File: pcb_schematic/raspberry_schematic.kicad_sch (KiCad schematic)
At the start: 13 parts, among them J1 Raspberry_Pi_2_3, SW1 SW_Push, SW2 SW_Push, SW3 SW_Push, SW4 SW_Push

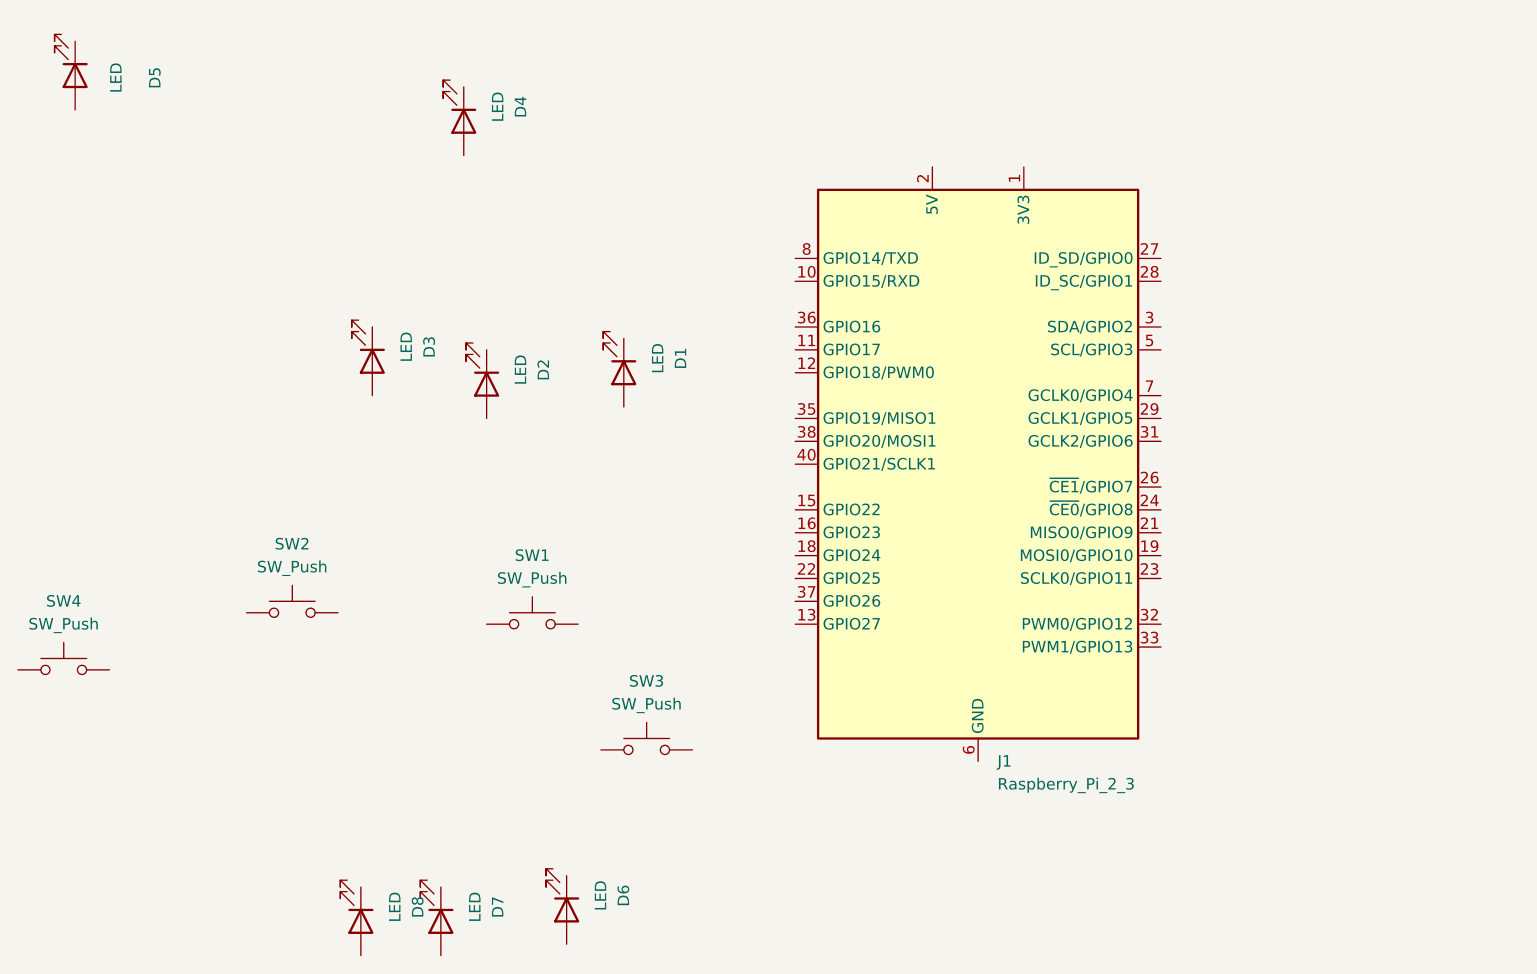
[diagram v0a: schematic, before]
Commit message: Finished raspberry schematic
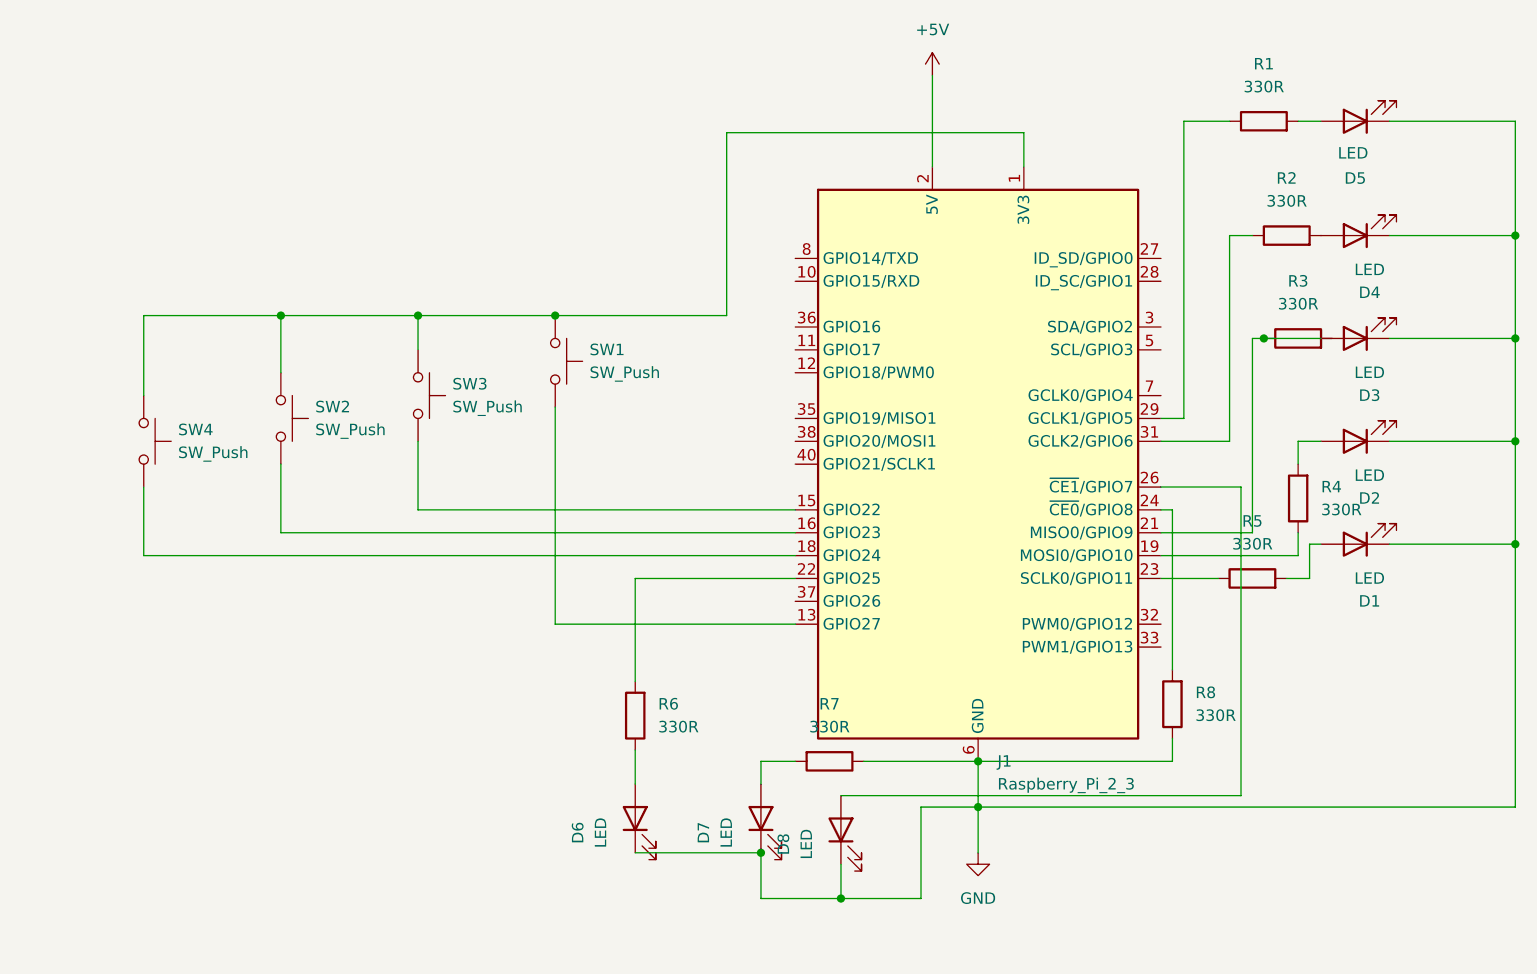
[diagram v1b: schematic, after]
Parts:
- added R1, R2, R3, R4, R5, R6, R7, R8: 330R, symbol Device:R
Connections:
- net at SW3.1: now also J1.1 (3V3), J1.17 (3V3), SW1.1, SW2.1, SW4.1
- net at SW3.2: now also J1.15 (GPIO22)
- net GND: now reaches D8.1 (K)
- net GND: now also D1.1 (K), D2.1 (K), D3.1 (K), D4.1 (K), D5.1 (K), D6.1 (K), D7.1 (K), J1.14 (GND), J1.20 (GND), J1.25 (GND), J1.30 (GND), J1.34 (GND), J1.39 (GND), J1.6 (GND), J1.9 (GND), R7.1, R8.1
- net at D8.2 (A): now also J1.26 (~{CE1}/GPIO7)
- net at D1.2 (A): now also R5.2
- net at D7.2 (A): now also R7.2
- net at D4.2 (A): now also R2.2
- net at D5.2 (A): now also R1.2
- net at D3.2 (A): now also J1.21 (MISO0/GPIO9), R3.1
- net at SW2.2: now also J1.16 (GPIO23)
- net at J1.13 (GPIO27): now also SW1.2
- net at J1.18 (GPIO24): now also SW4.2
- net at J1.19 (MOSI0/GPIO10): now also R4.1
- net +5V: now reaches J1.2 (5V), J1.4 (5V)
- net at J1.22 (GPIO25): now also R6.2
- net at J1.23 (SCLK0/GPIO11): now also R5.1
- net at J1.24 (~{CE0}/GPIO8): now also R8.2
- net at J1.29 (GCLK1/GPIO5): now also R1.1
- net at J1.31 (GCLK2/GPIO6): now also R2.1
- net at D6.2 (A): now also R6.1
- net at D2.2 (A): now also R4.2
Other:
- moved on the sheet: D1, D2, D3, D4, D5, D6, D7, D8, SW1, SW2, SW3, SW4

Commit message: Changed raspberry schematic to use currently available resistors
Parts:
- removed R6: 330R, symbol Device:R
- added R10, R11, R12, R13, R14, R15, R16, R9: 47R, symbol Device:R
- added R17, R18, R19: 10R, symbol Device:R
- R1, R2, R3, R4, R5, R8: value 330R -> 15R
- R7: value 330R -> 10R
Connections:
- net GND: now also R14.1, R17.1; no longer R7.1, R8.1
- net at D8.2 (A): now also R8.1; no longer J1.26 (~{CE1}/GPIO7)
- net at R5.1: now also R13.1; no longer J1.23 (SCLK0/GPIO11)
- net at R3.2: now also D3.2 (A)
- net at J1.24 (~{CE0}/GPIO8): now also R14.2; no longer R8.2
- net at J1.29 (GCLK1/GPIO5): now also R9.1; no longer R1.1
- net at J1.19 (MOSI0/GPIO10): now also R12.2; no longer R4.1
- net at J1.22 (GPIO25): now also R15.1
- net at J1.31 (GCLK2/GPIO6): now also R10.1; no longer R2.1
- net at D6.2 (A): now also R19.2
- new net: J1.23 (SCLK0/GPIO11), R13.2
- new net: R1.1, R9.2
- new net: R17.2, R7.1
- new net: R10.2, R2.1
- new net: R15.2, R18.1
- new net: R18.2, R19.1
- new net: J1.21 (MISO0/GPIO9), R11.1
- new net: J1.26 (~{CE1}/GPIO7), R16.2
- new net: R16.1, R8.2
- new net: R11.2, R3.1
- new net: R12.1, R4.1
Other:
- moved on the sheet: D1, D2, D3, R4, R5

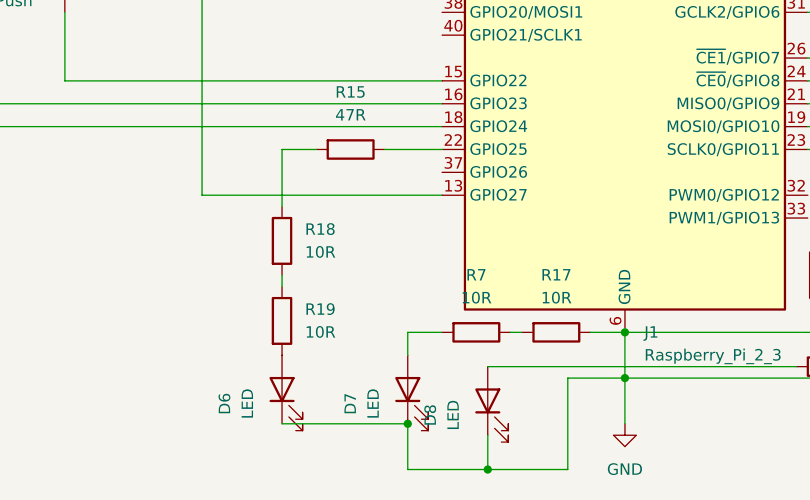
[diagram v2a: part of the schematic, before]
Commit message: Found 2 more 15 ohm resistors to use instead of 2 10 ohm resistors
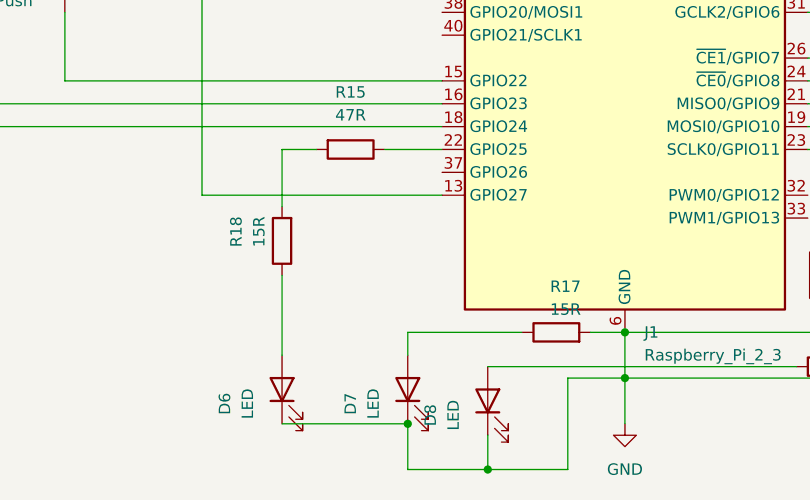
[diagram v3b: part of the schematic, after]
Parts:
- removed R19, R7: 10R, symbol Device:R
- R17, R18: value 10R -> 15R
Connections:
- net GND: now also R17.2; no longer R17.1
- net at D7.2 (A): now also R17.1
- net at R18.1: now also D6.2 (A); no longer R15.2
- net at R18.2: now also R15.2
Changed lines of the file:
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@@
-	(wire
-		(pts
-			(xy 154.94 142.24) (xy 156.21 142.24)
-		)
-		(stroke
-			(width 0)
-			(type default)
-		)
-	)
 	(wire
 		(pts
@@
 	(wire
 		(pts
+			(xy 129.54 135.89) (xy 129.54 144.78)
+		)
+		(stroke
+			(width 0)
+			(type default)
+		)
+	)
+	(wire
+		(pts
 			(xy 195.58 87.63) (xy 195.58 83.82)
 		)
@@
 	(wire
 		(pts
-			(xy 143.51 142.24) (xy 147.32 142.24)
-		)
-		(stroke
-			(width 0)
-			(type default)
-		)
-	)
-	(wire
-		(pts
-			(xy 129.54 135.89) (xy 129.54 137.16)
+			(xy 143.51 142.24) (xy 156.21 142.24)
 		)
 		(stroke
@@
 	)
 	(symbol
-		(lib_id "Device:R")
-		(at 160.02 142.24 270)
-		(unit 1)
-		(exclude_from_sim no)
-		(in_bom yes)
-		(on_board yes)
-		(dnp no)
-		(fields_autoplaced yes)
-		(property "Reference" "R17"
-			(at 160.02 135.89 90)
-			(effects
-				(font
-					(size 1.27 1.27)
-				)
-			)
-		)
-		(property "Value" "10R"
-			(at 160.02 138.43 90)
-			(effects
-				(font
-					(size 1.27 1.27)
-				)
-			)
-		)
-		(property "Footprint" ""
-			(at 160.02 140.462 90)
-			(effects
-				(font
-					(size 1.27 1.27)
-				)
-				(hide yes)
-			)
-		)
-		(property "Datasheet" "~"
-			(at 160.02 142.24 0)
-			(effects
-				(font
-					(size 1.27 1.27)
-				)
-				(hide yes)
-			)
-		)
-		(property "Description" "Resistor"
-			(at 160.02 142.24 0)
-			(effects
-				(font
-					(size 1.27 1.27)
-				)
-				(hide yes)
-			)
-		)
-		(pin "1"
-		)
-		(pin "2"
-		)
-		(instances
-			(project "raspberry_schematic"
-				(path "/b388c4a0-17e4-4175-bd7c-8be91d2c0837"
-					(reference "R17")
-					(unit 1)
-				)
-			)
-		)
-	)
-	(symbol
 		(lib_id "power:GND")
 		(at 167.64 152.4 0)
@@
 	(symbol
 		(lib_id "Device:R")
+		(at 129.54 132.08 180)
+		(unit 1)
+		(exclude_from_sim no)
+		(in_bom yes)
+		(on_board yes)
+		(dnp no)
+		(property "Reference" "R18"
+			(at 124.46 131.064 90)
+			(effects
+				(font
+					(size 1.27 1.27)
+				)
+			)
+		)
+		(property "Value" "15R"
+			(at 127 131.064 90)
+			(effects
+				(font
+					(size 1.27 1.27)
+				)
+			)
+		)
+		(property "Footprint" ""
+			(at 131.318 132.08 90)
+			(effects
+				(font
+					(size 1.27 1.27)
+				)
+				(hide yes)
+			)
+		)
+		(property "Datasheet" "~"
+			(at 129.54 132.08 0)
+			(effects
+				(font
+					(size 1.27 1.27)
+				)
+				(hide yes)
+			)
+		)
+		(property "Description" "Resistor"
+			(at 129.54 132.08 0)
+			(effects
+				(font
+					(size 1.27 1.27)
+				)
+				(hide yes)
+			)
+		)
+		(pin "1"
+		)
+		(pin "2"
+		)
+		(instances
+			(project "raspberry_schematic"
+				(path "/b388c4a0-17e4-4175-bd7c-8be91d2c0837"
+					(reference "R18")
+					(unit 1)
+				)
+			)
+		)
+	)
+	(symbol
+		(lib_id "Device:R")
 		(at 195.58 91.44 180)
 		(unit 1)
@@
 	)
 	(symbol
-		(lib_id "Device:R")
-		(at 151.13 142.24 270)
-		(unit 1)
-		(exclude_from_sim no)
-		(in_bom yes)
-		(on_board yes)
-		(dnp no)
-		(fields_autoplaced yes)
-		(property "Reference" "R7"
-			(at 151.13 135.89 90)
-			(effects
-				(font
-					(size 1.27 1.27)
-				)
-			)
-		)
-		(property "Value" "10R"
-			(at 151.13 138.43 90)
-			(effects
-				(font
-					(size 1.27 1.27)
-				)
-			)
-		)
-		(property "Footprint" ""
-			(at 151.13 140.462 90)
-			(effects
-				(font
-					(size 1.27 1.27)
-				)
-				(hide yes)
-			)
-		)
-		(property "Datasheet" "~"
-			(at 151.13 142.24 0)
-			(effects
-				(font
-					(size 1.27 1.27)
-				)
-				(hide yes)
-			)
-		)
-		(property "Description" "Resistor"
-			(at 151.13 142.24 0)
-			(effects
-				(font
-					(size 1.27 1.27)
-				)
-				(hide yes)
-			)
-		)
-		(pin "1"
-		)
-		(pin "2"
-		)
-		(instances
-			(project "raspberry_schematic"
-				(path "/b388c4a0-17e4-4175-bd7c-8be91d2c0837"
-					(reference "R7")
-					(unit 1)
-				)
-			)
-		)
-	)
-	(symbol
 		(lib_id "Device:LED")
 		(at 209.55 71.12 180)
@@
 	)
 	(symbol
-		(lib_id "Device:R")
-		(at 129.54 140.97 0)
-		(unit 1)
-		(exclude_from_sim no)
-		(in_bom yes)
-		(on_board yes)
-		(dnp no)
-		(fields_autoplaced yes)
-		(property "Reference" "R19"
-			(at 132.08 139.6999 0)
-			(effects
-				(font
-					(size 1.27 1.27)
-				)
-				(justify left)
-			)
-		)
-		(property "Value" "10R"
-			(at 132.08 142.2399 0)
-			(effects
-				(font
-					(size 1.27 1.27)
-				)
-				(justify left)
-			)
-		)
-		(property "Footprint" ""
-			(at 127.762 140.97 90)
-			(effects
-				(font
-					(size 1.27 1.27)
-				)
-				(hide yes)
-			)
-		)
-		(property "Datasheet" "~"
-			(at 129.54 140.97 0)
-			(effects
-				(font
-					(size 1.27 1.27)
-				)
-				(hide yes)
-			)
-		)
-		(property "Description" "Resistor"
-			(at 129.54 140.97 0)
-			(effects
-				(font
-					(size 1.27 1.27)
-				)
-				(hide yes)
-			)
-		)
-		(pin "1"
-		)
-		(pin "2"
-		)
-		(instances
-			(project "raspberry_schematic"
-				(path "/b388c4a0-17e4-4175-bd7c-8be91d2c0837"
-					(reference "R19")
-					(unit 1)
-				)
-			)
-		)
-	)
-	(symbol
 		(lib_id "Switch:SW_Push")
 		(at 90.17 104.14 270)
@@
 	(symbol
 		(lib_id "Device:R")
-		(at 129.54 132.08 0)
-		(unit 1)
-		(exclude_from_sim no)
-		(in_bom yes)
-		(on_board yes)
-		(dnp no)
-		(fields_autoplaced yes)
-		(property "Reference" "R18"
-			(at 132.08 130.8099 0)
-			(effects
-				(font
-					(size 1.27 1.27)
-				)
-				(justify left)
-			)
-		)
-		(property "Value" "10R"
-			(at 132.08 133.3499 0)
-			(effects
-				(font
-					(size 1.27 1.27)
-				)
-				(justify left)
-			)
-		)
-		(property "Footprint" ""
-			(at 127.762 132.08 90)
-			(effects
-				(font
-					(size 1.27 1.27)
-				)
-				(hide yes)
-			)
-		)
-		(property "Datasheet" "~"
-			(at 129.54 132.08 0)
-			(effects
-				(font
-					(size 1.27 1.27)
-				)
-				(hide yes)
-			)
-		)
-		(property "Description" "Resistor"
-			(at 129.54 132.08 0)
-			(effects
-				(font
-					(size 1.27 1.27)
-				)
-				(hide yes)
-			)
-		)
-		(pin "1"
-		)
-		(pin "2"
-		)
-		(instances
-			(project "raspberry_schematic"
-				(path "/b388c4a0-17e4-4175-bd7c-8be91d2c0837"
-					(reference "R18")
-					(unit 1)
-				)
-			)
-		)
-	)
-	(symbol
-		(lib_id "Device:R")
 		(at 189.23 135.89 180)
 		(unit 1)
@@
 					(unit 1)
 				)
+			)
+		)
+	)
+	(symbol
+		(lib_id "Device:R")
+		(at 160.02 142.24 90)
+		(unit 1)
+		(exclude_from_sim no)
+		(in_bom yes)
+		(on_board yes)
+		(dnp no)
+		(property "Reference" "R17"
+			(at 161.036 137.16 90)
+			(effects
+				(font
+					(size 1.27 1.27)
+				)
+			)
+		)
+		(property "Value" "15R"
+			(at 161.036 139.7 90)
+			(effects
+				(font
+					(size 1.27 1.27)
+				)
+			)
+		)
+		(property "Footprint" ""
+			(at 160.02 144.018 90)
+			(effects
+				(font
+					(size 1.27 1.27)
+				)
+				(hide yes)
+			)
+		)
+		(property "Datasheet" "~"
+			(at 160.02 142.24 0)
+			(effects
+				(font
+					(size 1.27 1.27)
+				)
+				(hide yes)
+			)
+		)
+		(property "Description" "Resistor"
+			(at 160.02 142.24 0)
+			(effects
+				(font
+					(size 1.27 1.27)
+				)
+				(hide yes)
+			)
+		)
+		(pin "1"
+		)
+		(pin "2"
+		)
+		(instances
+			(project "raspberry_schematic"
+				(path "/b388c4a0-17e4-4175-bd7c-8be91d2c0837"
+					(reference "R17")
+					(unit 1)
+				)
